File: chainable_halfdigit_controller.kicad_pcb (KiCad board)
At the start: 2 copper layers, 100 x 35 mm, 9 parts, among them J1 USB_OTG, J2 Conn_01x06, U1 NRF24L01, U2 arduino_nano

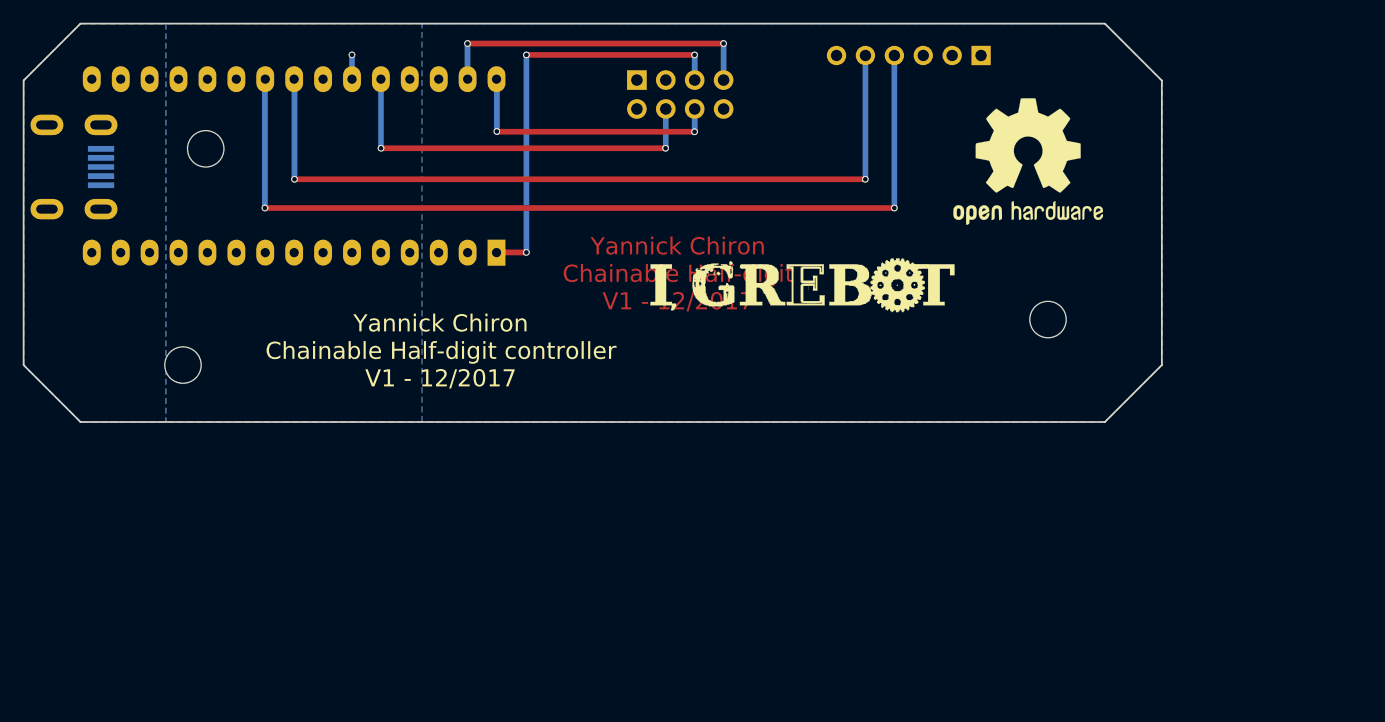
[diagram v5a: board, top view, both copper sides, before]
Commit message: Added banana jack and pin header for power switch
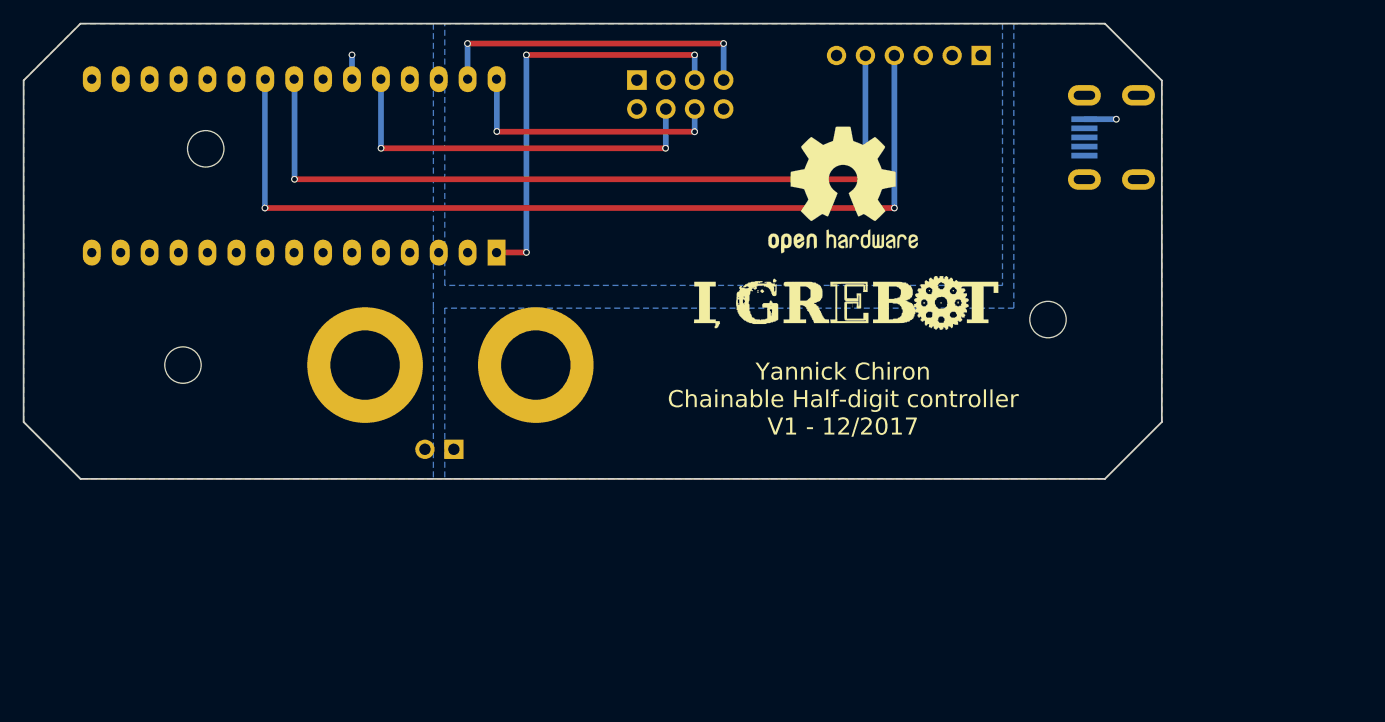
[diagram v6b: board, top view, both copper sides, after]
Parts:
- added J3: Conn_01x01, Connectors:Banana_Jack_1Pin, B.Cu at (95.0, 80.0)
- added J4: Conn_01x01, Connectors:Banana_Jack_1Pin, B.Cu at (80.0, 80.0)
- added SW1: SW_SPST, Pin_Headers:Pin_Header_Straight_1x02_Pitch2.54mm, B.Cu at (87.8, 87.4)
- moved J1 86.4 mm to (143.2, 60.0), turned to 90 degrees
- moved REF*** 16.4 mm to (122.0, 64.6)
- moved G*** 4.14 mm to (122.0, 74.0)
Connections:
- J1 pad 1: 5V -> +5V
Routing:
- net +5V: track 0.00 -> 2.80 mm, vias 0 -> 1
- added copper zone on B.Cu, net +5V
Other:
- board size 100 x 35 mm -> 100 x 40 mm
- board text removed: "Yannick Chiron Chainable Half-digit V1 - 12/2017"
